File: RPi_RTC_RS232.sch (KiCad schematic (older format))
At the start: 0 parts

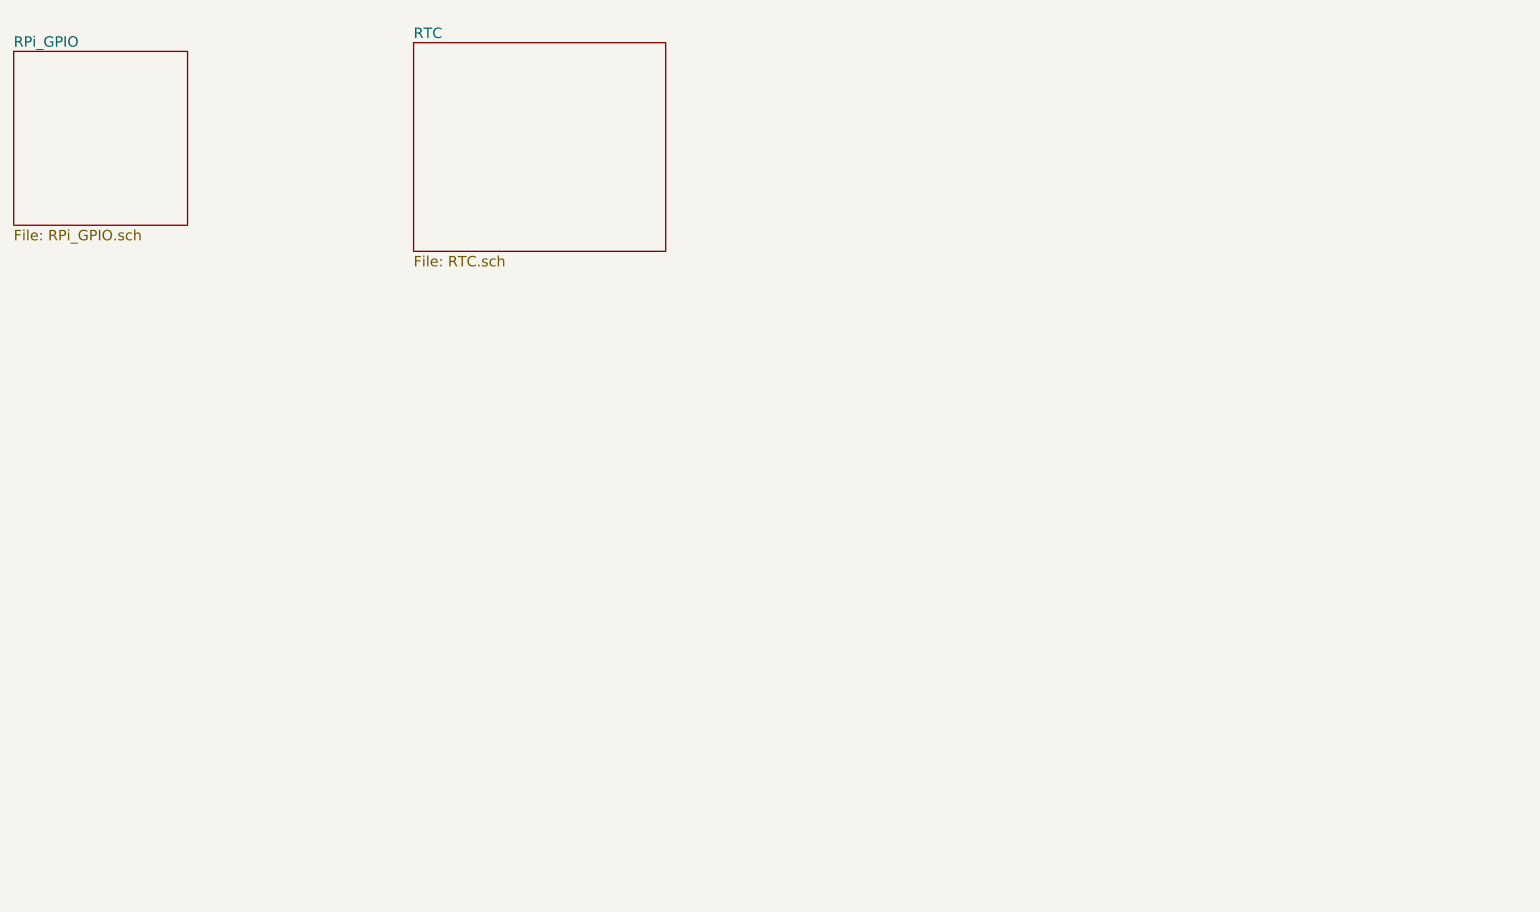
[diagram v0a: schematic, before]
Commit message: schematic and provisional layout for RTC and RS232
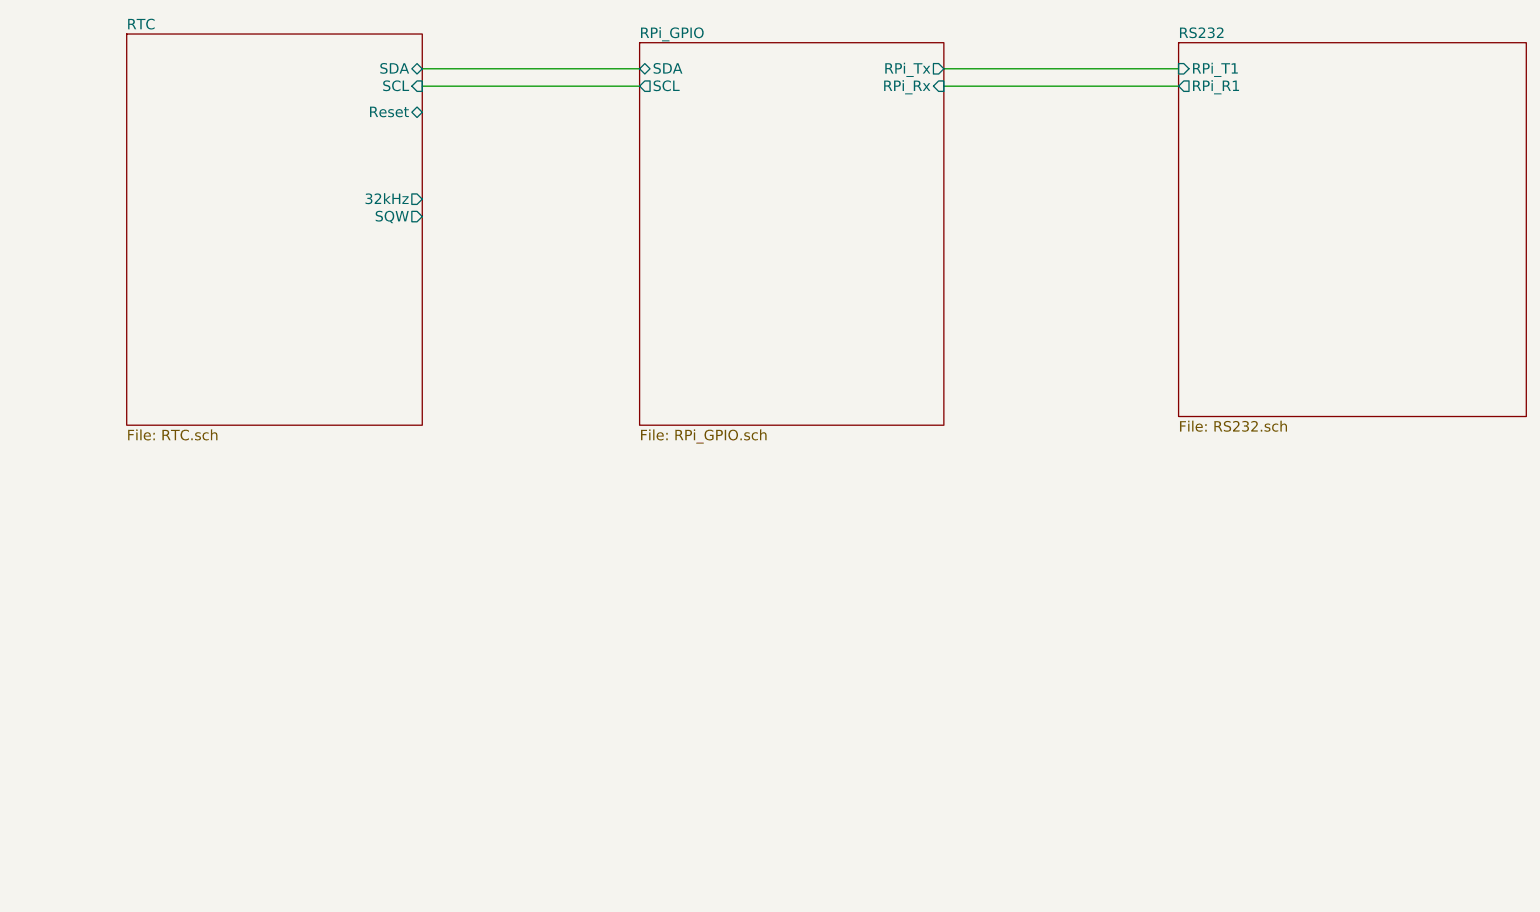
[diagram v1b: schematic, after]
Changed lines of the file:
@@
 $Descr A4 11693 8268
 encoding utf-8
-Sheet 1 3
+Sheet 1 4
 Title ""
 Date ""
@@
 $EndDescr
 $Sheet
-S 1400 1400 1000 1000
+S 5000 1350 1750 2200
 U 5515D395
 F0 "RPi_GPIO" 60
 F1 "RPi_GPIO.sch" 60
+F2 "SDA" B L 5000 1500 60
+F3 "SCL" O L 5000 1600 60
+F4 "RPi_Tx" O R 6750 1500 60
+F5 "RPi_Rx" I R 6750 1600 60
 $EndSheet
 $Sheet
-S 3700 1350 1450 1200
+S 2050 1300 1700 2250
 U 5559D4CA
 F0 "RTC" 60
 F1 "RTC.sch" 60
+F2 "SQW" O R 3750 2350 60
+F3 "32kHz" O R 3750 2250 60
+F4 "SCL" I R 3750 1600 60
+F5 "SDA" B R 3750 1500 60
+F6 "Reset" B R 3750 1750 60
 $EndSheet
+$Sheet
+S 8100 1350 2000 2150
+U 555B01F7
+F0 "RS232" 60
+F1 "RS232.sch" 60
+F2 "RPi_T1" I L 8100 1500 60
+F3 "RPi_R1" O L 8100 1600 60
+$EndSheet
+Wire Wire Line
+	3750 1500 5000 1500
+Wire Wire Line
+	5000 1600 3750 1600
+Wire Wire Line
+	8100 1500 6750 1500
+Wire Wire Line
+	6750 1600 8100 1600
 $EndSCHEMATC

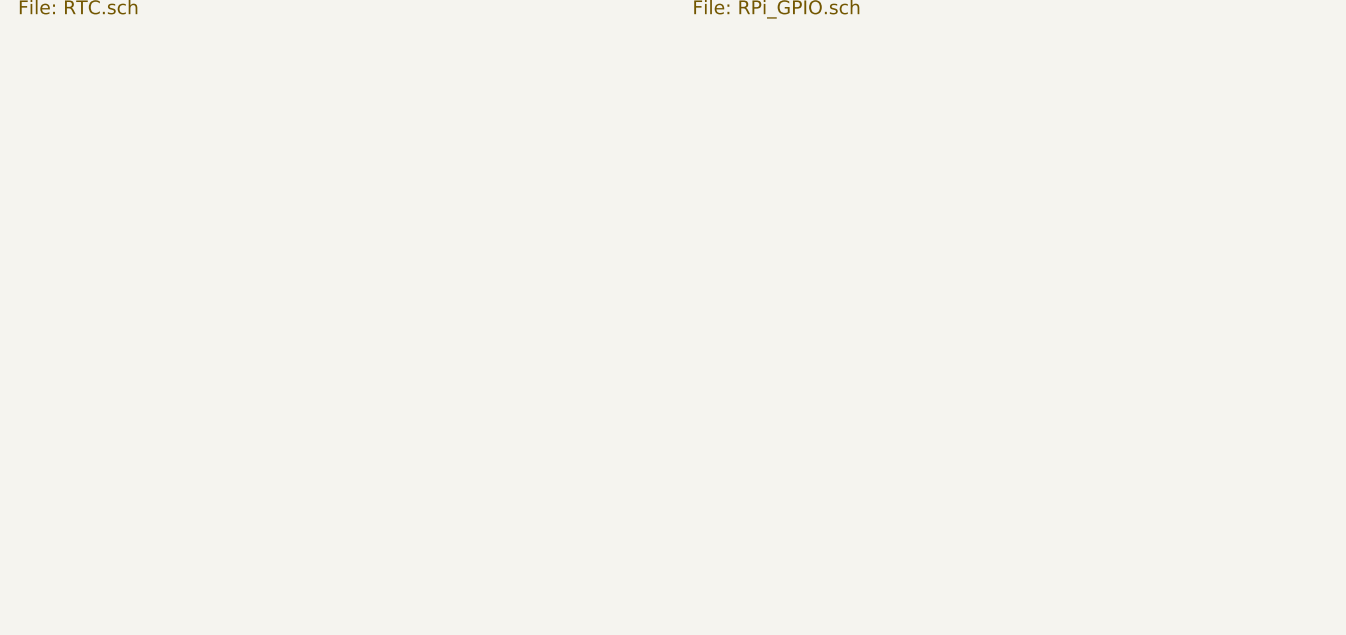
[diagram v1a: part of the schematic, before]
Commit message: added power and nimh charge IC TODO charge circuit
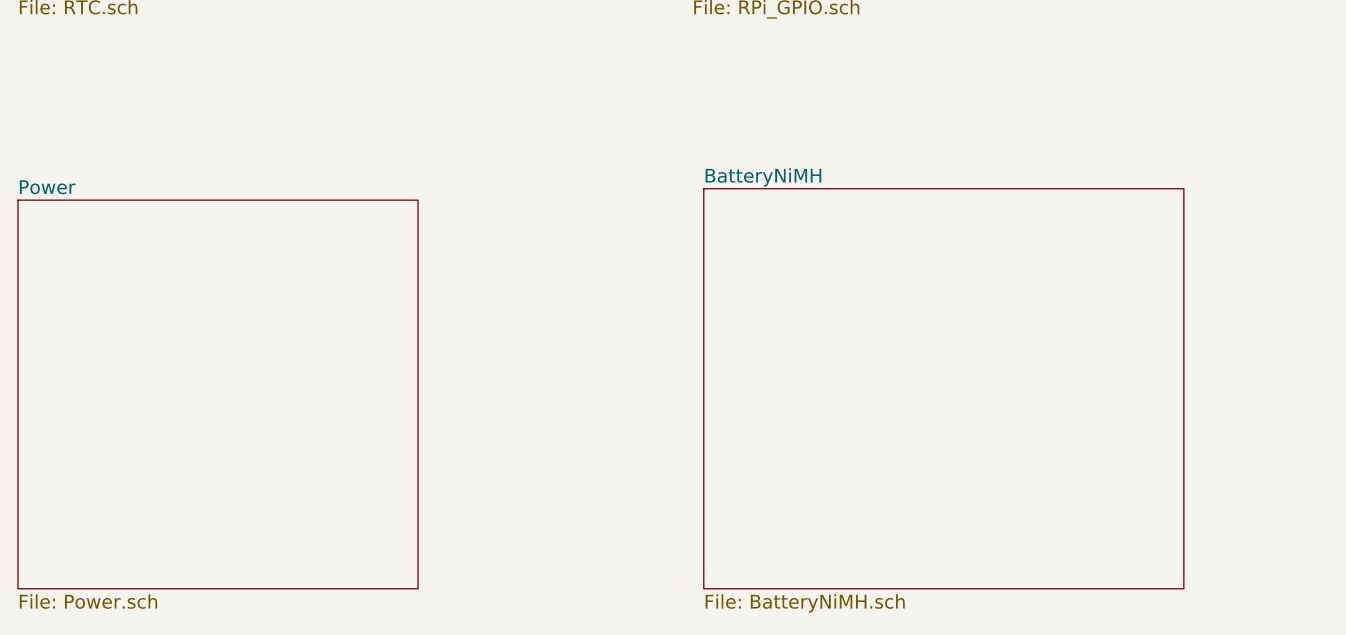
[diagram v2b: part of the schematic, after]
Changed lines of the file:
@@
 LIBS:maxim
 LIBS:Ben
+LIBS:DS2715
 LIBS:RPi_RTC_RS232-cache
 EELAYER 25 0
@@
 $Descr A4 11693 8268
 encoding utf-8
-Sheet 1 4
+Sheet 1 6
 Title ""
 Date ""
@@
 Wire Wire Line
 	6750 1600 8100 1600
+$Sheet
+S 2050 4450 1750 1700
+U 555B8D90
+F0 "Power" 60
+F1 "Power.sch" 60
+$EndSheet
+$Sheet
+S 5050 4400 2100 1750
+U 555CBA49
+F0 "BatteryNiMH" 60
+F1 "BatteryNiMH.sch" 60
+$EndSheet
 $EndSCHEMATC
